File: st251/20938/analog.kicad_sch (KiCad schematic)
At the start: 202 parts, among them J1 control, J2 data, J3 POWER, J4 SPINDLE, J5 STEPPER, J6 HEADS, J7 CONFIG, Q1 BC859, Q2 2SD1760, Q3 IRFD110, Q4 IRFD110, Q5 IRFD110

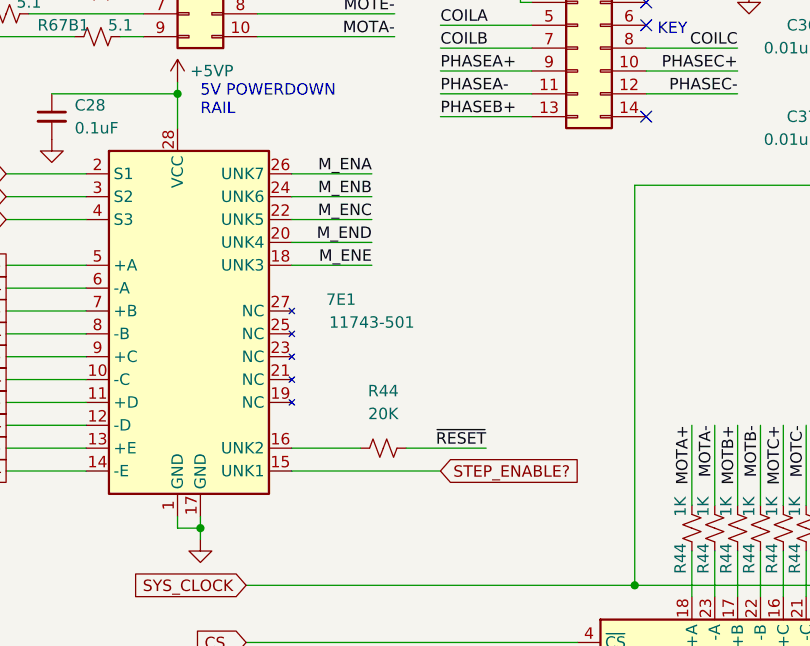
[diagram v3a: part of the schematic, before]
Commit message: Add 11743-501 description (stepper enable driver)
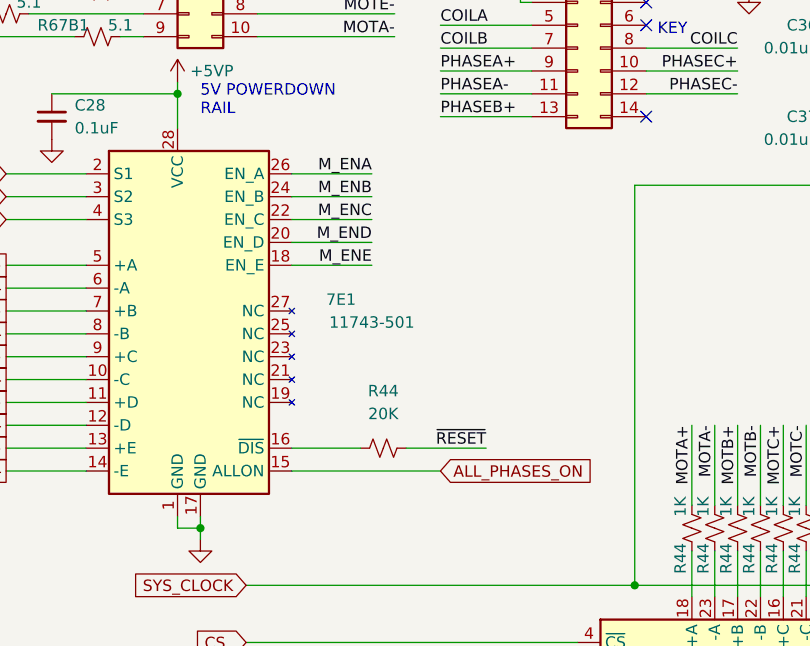
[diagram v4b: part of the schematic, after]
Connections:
- net STEP_ENABLE? renamed ALL_PHASES_ON
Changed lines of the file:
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@@
     )
   )
-  (global_label "STEP_ENABLE?" (shape input) (at 138.43 236.22 0) (fields_autoplaced)
+  (global_label "ALL_PHASES_ON" (shape input) (at 138.43 236.22 0) (fields_autoplaced)
     (effects (font (size 1.27 1.27)) (justify left))
-    (property "Intersheetrefs" "${INTERSHEET_REFS}" (at 155.0827 236.22 0)
+    (property "Intersheetrefs" "${INTERSHEET_REFS}" (at 156.4133 236.22 0)
       (effects (font (size 1.27 1.27)) (justify left) hide)
     )

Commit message: Add ring detector LSI docs
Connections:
- net INDEX_SYNC renamed ~{INDEX_SYNC}
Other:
- moved on the sheet: C27, C41, C62, CR4, D1, Q2, R44

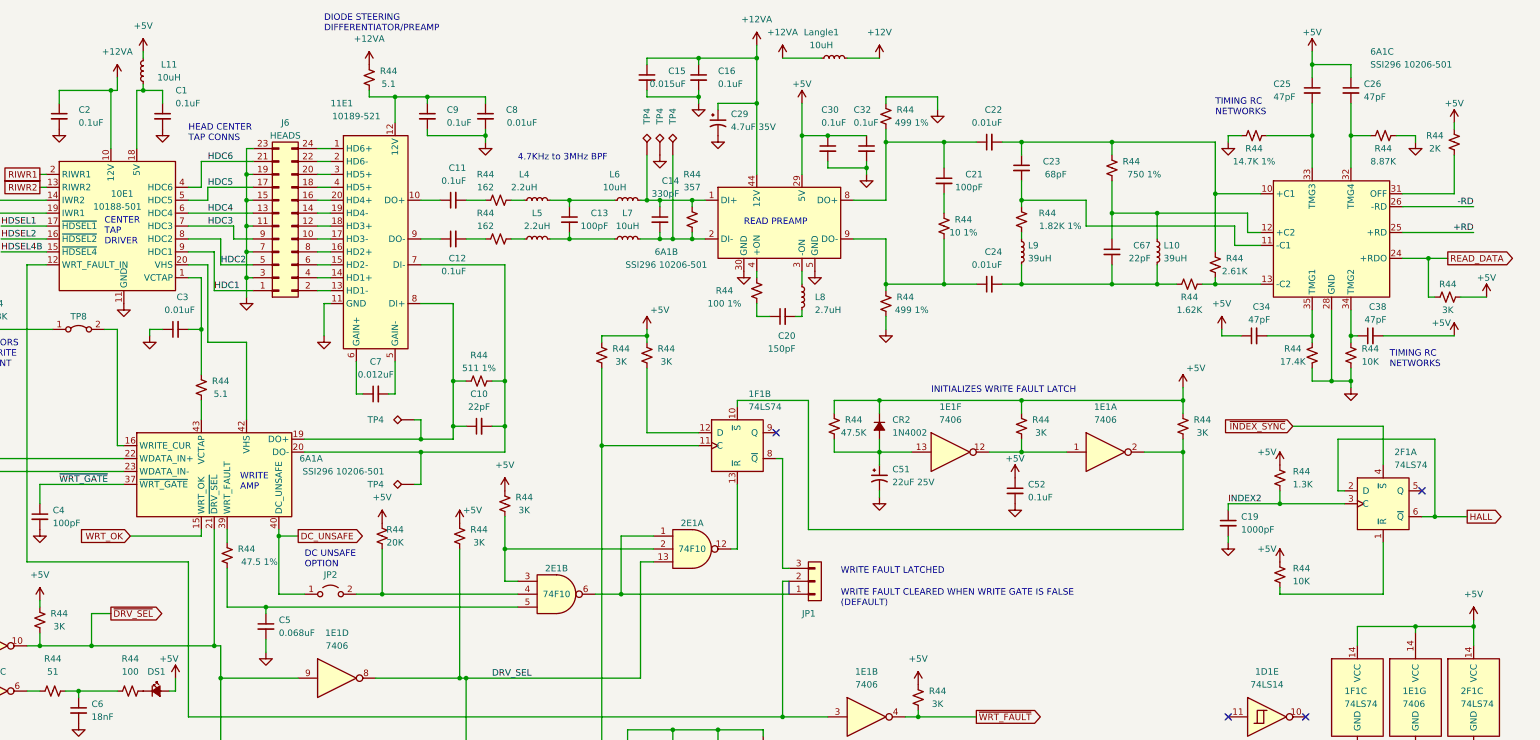
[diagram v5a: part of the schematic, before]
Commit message: Add read channel IC
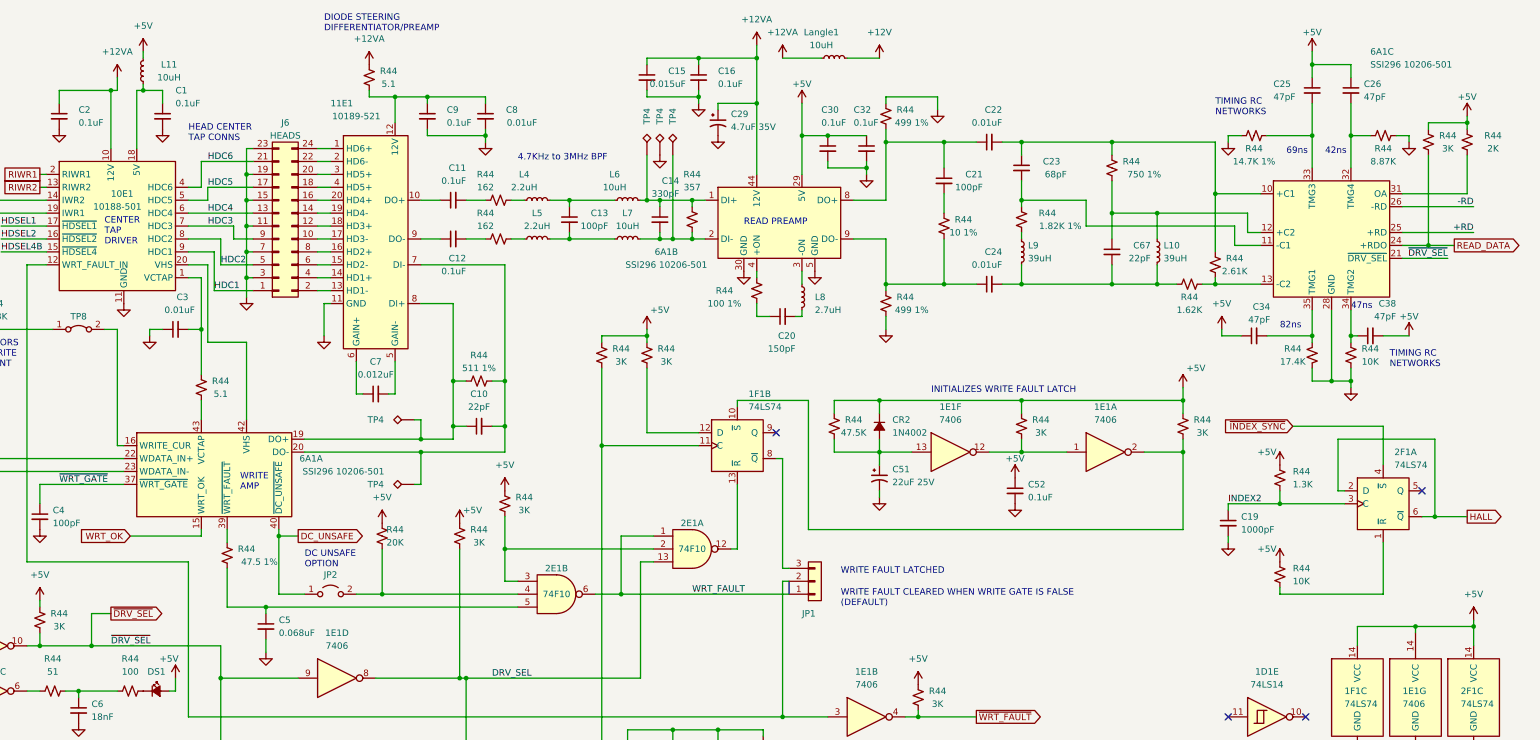
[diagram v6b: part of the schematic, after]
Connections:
- net ~{DRV_SEL}: now also 6A1.21 (~{DRV_SEL}); no longer 6A1.21 (~{DRV_SEL})
- net WRT_FAULT: now reaches 2E1.1, 2E1.6, JP1.1 (Pin_1)
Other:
- note added: "42ns"
- note added: "47ns"
- note added: "69ns"
- note added: "82ns"
- moved on the sheet: R44

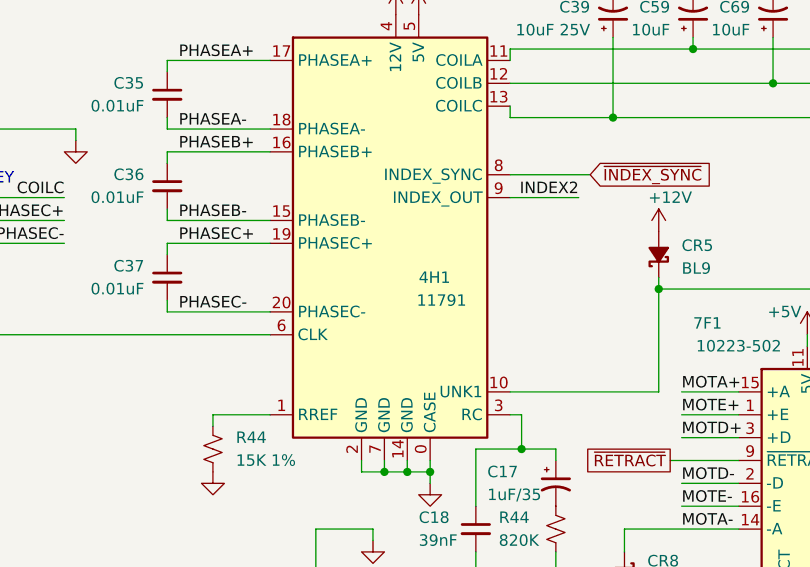
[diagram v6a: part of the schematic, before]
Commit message: fix some spindle motor driver pins
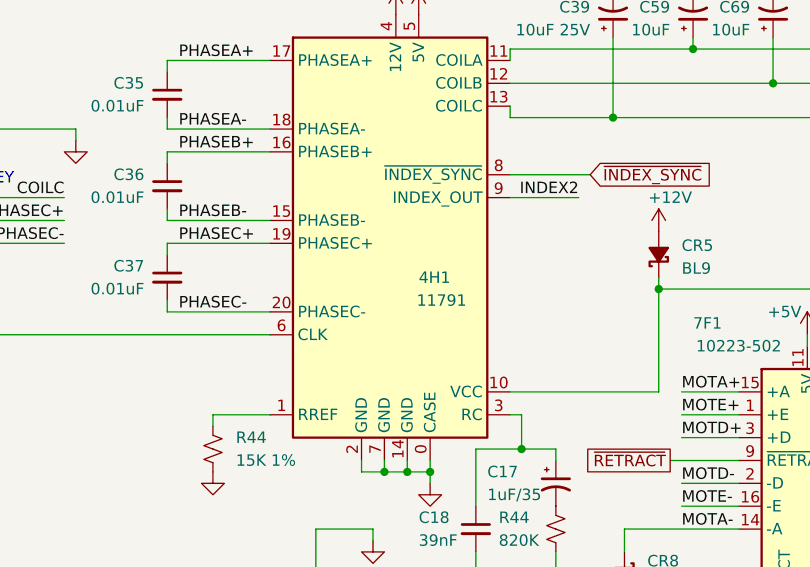
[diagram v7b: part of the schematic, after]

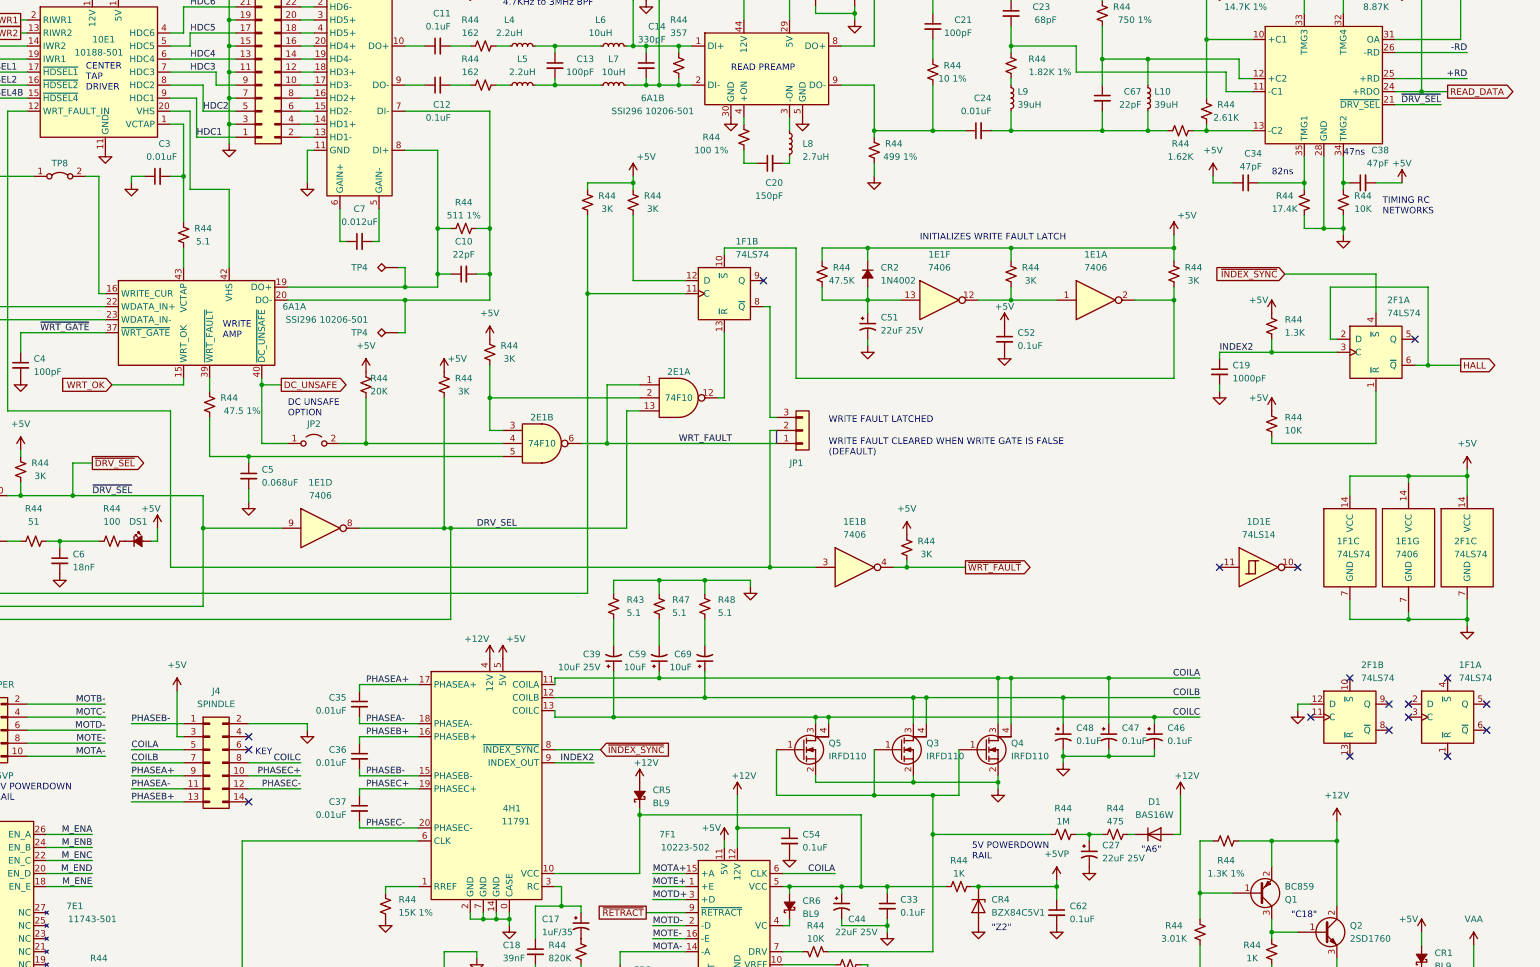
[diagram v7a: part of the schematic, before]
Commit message: fix 20938 spindle motor wiring net names
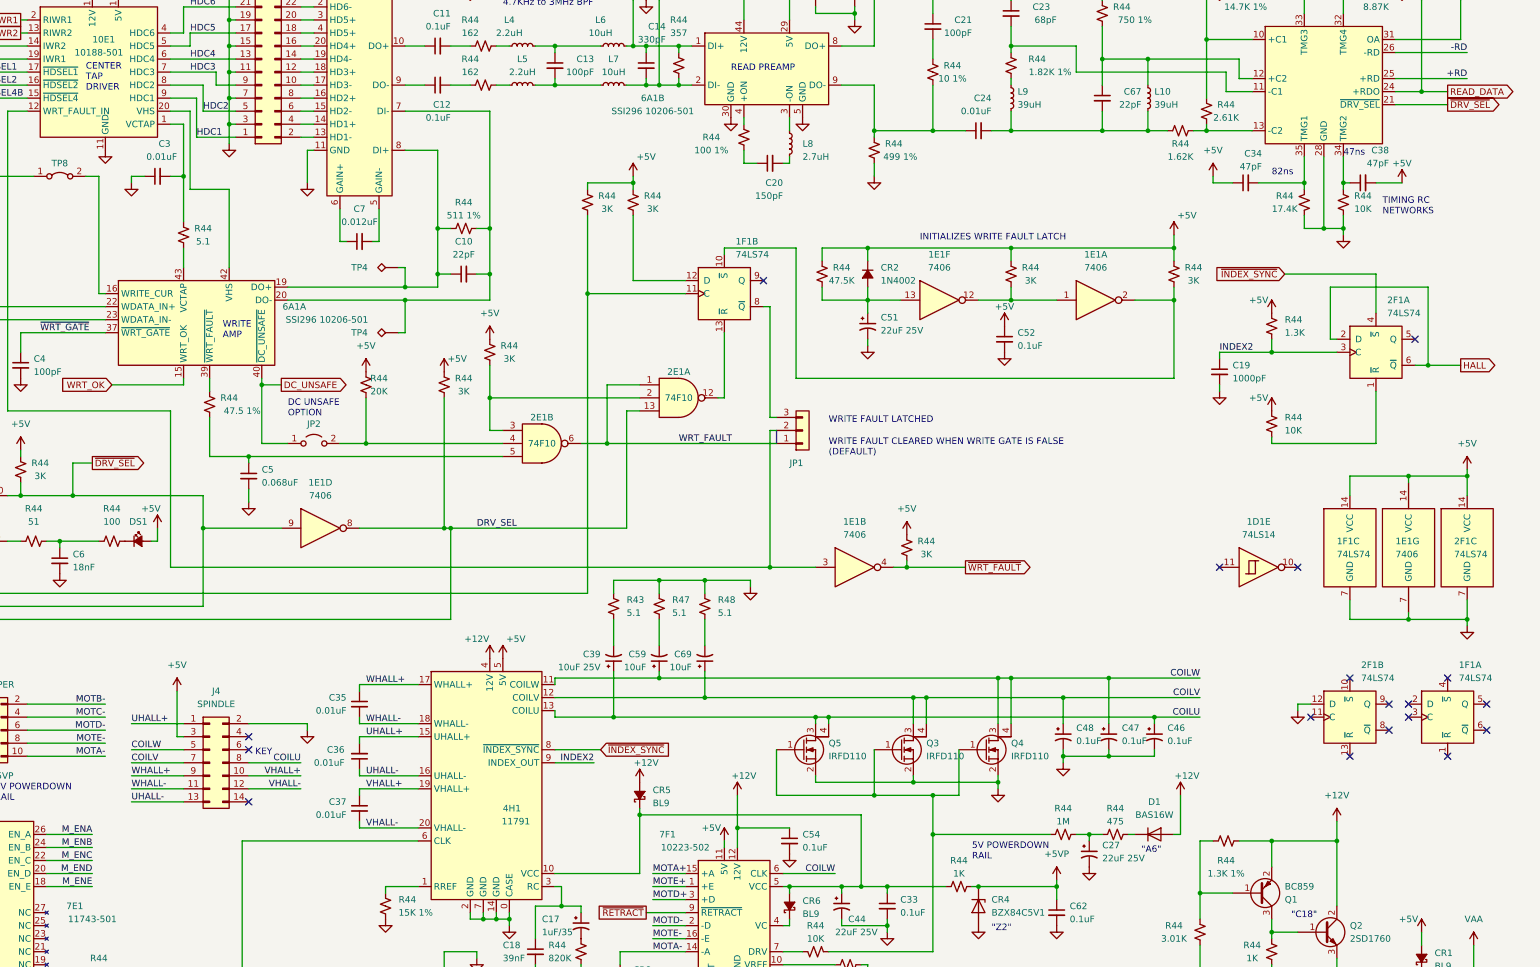
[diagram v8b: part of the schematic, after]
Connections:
- net COILA renamed COILW
- net COILB renamed COILV
- net COILC renamed COILU
- net PHASEA+ renamed WHALL+
- net PHASEA- renamed WHALL-
- net PHASEB+ renamed UHALL-
- net PHASEB- renamed UHALL+
- net PHASEC+ renamed VHALL+
- net PHASEC- renamed VHALL-
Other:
- moved on the sheet: C36
